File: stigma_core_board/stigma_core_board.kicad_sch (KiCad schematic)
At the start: 83 parts, among them J1 TC2050, J5 USB_C_Receptacle_USB2.0, SW1 KMR721NGLFS, SW2 KMR721NGLFS, U1 STM32H743VITx, U10 H3LIS331DL, U11 MS5607/MS5611, U12 LIS3MDL, U13 BMP580/BMP388/LPS22, U2 TPD4E1U06, U3 BMP580/BMP388/LPS22, U4 IIM-42652 (or other LGA-14 IM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, U5 AZ1117I-3.3, U6 ICM-42688 (or other LGA-14 IM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, U8 W25Q128JVP, U9 LSM6DSR, Y1 25MHz, Y2 32.768kHz

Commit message: Restore stigma_core_board from 4524638
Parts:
- added C39, C40: 100n, Capacitor_SMD:C_0402_1005Metric, symbol Device:C_Small
- added R14: 4k7, Resistor_SMD:R_0402_1005Metric, symbol Device:R_Small
- added R15: 10k, Resistor_SMD:R_0402_1005Metric, symbol Device:R_Small
- added R16, R17, R18, R19, R20: 22, Resistor_SMD:R_0402_1005Metric, symbol Device:R_Small
- added U7: TPD4E1U06, Package_TO_SOT_SMD:SOT-563, symbol stigma:TPD4E001DRL
- C1: LCSC (none) -> C19666
- C10, C9: LCSC (none) -> C12530
- C11, C12: value 3.9p -> 10p; LCSC (none) -> C32949
- C13, C14: value 1.5p -> 10p; LCSC (none) -> C32949
- C15, C20, C21, C22, C24, C25, C27, C28, C29, C30, C31, C34, C35, C36: LCSC (none) -> C1525; LCSC# C1591 -> (none)
- C16, C17, C3, C4, C5, C6, C7: LCSC (none) -> C1525
- C18, C23: LCSC (none) -> C19702; LCSC# C14860 -> (none)
- C19: LCSC (none) -> C86295; LCSC# C12891 -> (none)
- C2, C8: LCSC (none) -> C28323
- C26, C33, C37: LCSC (none) -> C28323; LCSC# C318694 -> (none)
- C32, C38: LCSC (none) -> C15195; LCSC# C1591 -> (none)
- D1: value LED_Small -> red; LCSC (none) -> C2286
- D2: value LED_Small -> yellow; LCSC (none) -> C2296
- D3: value LED_Small -> green; LCSC (none) -> C2297
- D4: footprint Diode_SMD:D_SOD-123F -> Diode_SMD:D_SOD-123; LCSC (none) -> C8598; LCSC# C167645 -> (none)
- FB1: LCSC (none) -> C1002
- J3: footprint stigma:DF40GB-70DP-0.4V -> stigma:DF40GB-70DP-0.4V-plug; symbol Connector_Generic:Conn_02x35_Top_Bottom -> Connector_Generic_Shielded:Conn_02x35_Top_Bottom_Shielded; now left out of the parts list
- J5: LCSC (none) -> C709357; LCSC# C709357 -> (none)
- R1, R2, R3, R4: LCSC (none) -> C17168
- R10, R11: LCSC (none) -> C25905; LCSC# C105580 -> (none)
- R12, R13: value 22 -> 22R; LCSC (none) -> C25092; LCSC# C107701 -> (none)
- R5: LCSC (none) -> C25741; LCSC# C98220 -> (none)
- R6: LCSC (none) -> C11702; LCSC# C98220 -> (none)
- R7, R8, R9: value 680 -> 1k; LCSC (none) -> C11702
- SW1, SW2: LCSC (none) -> C2911418; LCSC# C2911418 -> (none)
- U1: LCSC (none) -> C730183
- U10: LCSC (none) -> C2655074
- U11: LCSC (none) -> C97627
- U12: LCSC (none) -> C478483; LCSC# C478483 -> (none)
- U13: value BMP580/BMP388/LPS22 -> BMP580; LCSC (none) -> C22391138
- U2: footprint Package_TO_SOT_SMD:SOT-23-6 -> Package_TO_SOT_SMD:SOT-563; symbol Power_Protection:SRV05-4 -> stigma:TPD4E001DRL; LCSC (none) -> C527516
- U3: value BMP580/BMP388/LPS22 -> LPS22; LCSC (none) -> C2827824
- U4: value IIM-42652 (or other LGA-14 IMU) -> ICM-42670-P; LCSC (none) -> C3288646; LCSC# C784817 -> (none); Manufacturer STMicroelectronics -> (none); Part# LSM6DSRTR -> (none)
- U5: LCSC (none) -> C92102; LCSC# C92102 -> (none)
- U6: value ICM-42688 (or other LGA-14 IMU) -> ICM-42688-P; LCSC (none) -> C1850418; LCSC# C784817 -> (none)
- U8: LCSC (none) -> C190862
- U9: LCSC (none) -> C784817; LCSC# C784817 -> (none)
- Y1: LCSC (none) -> C9006
- Y2: LCSC (none) -> C70509
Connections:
- net +3V3 is gone; now on net +3.3V: C19.2, C21.2, C22.2, C23.2, C24.2, C25.2, C26.2, C27.2, C29.2, C30.2, C31.2, C32.2, C33.2, C34.2, C35.2, C36.2, C37.2, C38.2, R6.2, U10.1 (VDD_{IO}), U10.14 (VDD), U10.15 (reserved), U11.1 (VDD), U12.5 (Vdd), U12.6 (Vdd_IO), U13.1 (VDDIO), U13.10 (VDD), U3.1 (VDDIO), U3.10 (VDD), U4.5 (VDDIO), U4.8 (VDD), U5.2 (VO), U6.5 (VDDIO), U6.8 (VDD), U9.5 (VDDIO), U9.8 (VDD)
- net ETH_CRS_DV is gone; now on net PA7_ETH_CRS_DV: U1.31 (PA7)
- net ETH_MDC is gone; now on net PC1_ETH_MDC: U1.16 (PC1)
- net ETH_MDIO is gone; now on net PA2_ETH_MDIO: U1.24 (PA2)
- net ETH_RXD0 is gone; now on net ETH_RXD-: U1.32 (PC4)
- net ETH_RXD1 is gone; now on net ETH_RXD+: U1.33 (PC5)
- net ETH_TXD0 is gone; now on net ETH_TXD-: U1.51 (PB12)
- net ETH_TXD1 is gone; now on net ETH_TXD+: U1.52 (PB13)
- net ETH_TX_EN is gone; now on net PB11_ETH_TX_EN: U1.47 (PB11)
- net PA0_U4TX_T2/1_T5/1_ADC is gone; now on net PA0: U1.22 (PA0)
- net PA10_T1/3_U1RX is gone; now on net LED_YELLOW: U1.69 (PA10)
- net PA15_T2/1_U7TX is gone; now on net LED_GREEN: U1.77 (PA15)
- net PA3_U2RX_T2/4_T5/4_T15/2_ADC is gone; now on net PA3: U1.25 (PA3)
- net PA4_ADC_DAC is gone; now on net PA4: U1.28 (PA4)
- net PA8_T1/1_I3SCL_U7RX is gone; now on net LED_RED: U1.67 (PA8)
- net PB0_T1/2N_T3/3_T8/2N_ADC is gone; now on net PB0: U1.34 (PB0)
- net PB10_T2/3_I2SCL_(SPI2_SCK)_U3TX is gone; now on net PB10: U1.46 (PB10)
- net PB1_T1/3N_T3/4_T8/3N_ADC is gone; now on net PB1: U1.35 (PB1)
- net PB4_T3/1_(SPI1_MISO, SPI3_MISO, SPI6_MISO)_U7TX is gone; now on net SPI1_MISO: U1.90 (PB4)
- net PB7_T17/1N_T4/2_I1SDA_I4SDA_U1RX is gone; now on net PB7: U1.93 (PB7)
- net PB8_T16/1_T4/3_I1SCL_I4SCL_U4RX_(CAN1_RX) is gone; now on net PB8: U1.95 (PB8)
- net PB9_T17/1_T4/4_I1SDA_I4SDA_U4TX_(CAN1_TX) is gone; now on net PB9: U1.96 (PB9)
- net SPI1_CS_ACC is gone; now on net SPI1_CS_HIGHG: U10.8 (~{CS})
- net SPI1_CS_BARO2 is gone; now on net SPI2_CS_BARO2: U3.6 (~{CS})
- net SPI1_CS_BARO3 is gone; now on net SPI2_CS_BARO3: U13.6 (~{CS})
- net SPI1_CS_IMU2 is gone; now on net SPI2_CS_IMU2: U6.12 (CS)
- net SPI1_CS_IMU3 is gone; now on net SPI2_CS_IMU3: U4.12 (CS)
- net SPI1_SCL is gone; now on net SPI1_SCK: U10.4 (SCK), U11.8 (SCLK), U12.1 (SCL/SPC), U9.13 (SCL)
- net SPI4_MISO is gone; now on net PE5: U1.4 (PE5)
- net SPI4_MOSI is gone; now on net PE6: U1.5 (PE6)
- net SPI4_SCK is gone; now on net PE2: U1.1 (PE2)
- net +3.3V: now also U7.5 (IO4)
- net +5V: now also J3.1 (Pin_1), J3.2 (Pin_2), J3.34 (Pin_34), J3.35 (Pin_35), J3.36 (Pin_36), J3.37 (Pin_37), J3.69 (Pin_69), J3.70 (Pin_70), C39.2, U7.6 (V_{cc})
- net BOOT: now also U2.1 (IO1), R20.1
- net D0+: now also U2.4 (IO3); no longer U2.6 (IO4)
- net D0-: now also U2.5 (IO4); no longer U2.4 (IO3)
- net GND: now also J3.18 (Pin_18), J3.26 (Pin_26), J3.3 (Pin_3), J3.30 (Pin_30), J3.33 (Pin_33), J3.38 (Pin_38), J3.45 (Pin_45), J3.53 (Pin_53), J3.58 (Pin_58), J3.68 (Pin_68), J3.SH (Shield), U2.3 (GND), C39.1, C40.1, R15.1, U7.3 (GND); no longer J3.25 (Pin_25), J3.28 (Pin_28), J3.44 (Pin_44), J3.60 (Pin_60), U2.2 (VN)
- net NRST: now also U2.2 (IO2), R17.1; no longer U1.14 (NRST)
- net SPI1_CS_BARO1: now also U1.83 (PD2)
- net SPI1_CS_IMU1: now also U1.85 (PD4)
- net SPI1_CS_MAG: now also U1.86 (PD5)
- net SPI1_MISO: no longer U1.30 (PA6)
- net SPI2_MISO: now also U1.53 (PB14); no longer U1.17 (PC2_C)
- net SPI2_MOSI: now also U1.54 (PB15); no longer U1.18 (PC3_C)
- net SPI3_CS_FLASH: now also U1.87 (PD6)
- net SPI3_MISO: now also J3.24 (Pin_24)
- net SPI3_MOSI: now also J3.25 (Pin_25)
- net SPI3_SCK: now also J3.23 (Pin_23)
- net SWCLK: now also R16.2; no longer J1.6 (Pin_6)
- net SWDIO: now also R18.1; no longer J1.2 (Pin_2)
- net SWO: now also R19.1; no longer J1.5 (Pin_5)
- net USB_FS_VBUS: now also R14.1, R15.2
- net VCAP1: now reaches C9.1, U1.48 (VCAP)
- net PC0: now reaches U1.15 (PC0)
- net PC0: now also J3.67 (Pin_67)
- net SPI2_CS_BARO3: now reaches U1.2 (PE3)
- net SPI2_CS_BARO2: now reaches U1.3 (PE4)
- net PE7: now reaches U1.37 (PE7)
- net PE7: now also J3.10 (Pin_10)
- net PE8: now reaches U1.38 (PE8)
- net PE8: now also J3.11 (Pin_11)
- net PE9: now reaches U1.39 (PE9)
- net PE9: now also J3.12 (Pin_12)
- net PE10: now reaches U1.40 (PE10)
- net PE10: now also J3.13 (Pin_13)
- net PE11: now reaches U1.41 (PE11)
- net PE11: now also J3.14 (Pin_14)
- net PE12: now reaches U1.42 (PE12)
- net PE12: now also J3.15 (Pin_15)
- net PE13: now reaches U1.43 (PE13)
- net PE13: now also J3.16 (Pin_16)
- net PE14: now reaches U1.44 (PE14)
- net PE14: now also J3.17 (Pin_17)
- net SPI2_CS_IMU2: now reaches U1.55 (PD8)
- net SPI1_CS_HIGHG: now reaches U1.56 (PD9)
- net PD12: now reaches U1.59 (PD12)
- net PD12: now also J3.41 (Pin_41)
- net PD13: now reaches U1.60 (PD13)
- net PD13: now also J3.42 (Pin_42)
- net PD14: now reaches U1.61 (PD14)
- net PD14: now also J3.43 (Pin_43)
- net PD15: now reaches U1.62 (PD15)
- net PD15: now also J3.44 (Pin_44)
- net PC6: now reaches U1.63 (PC6)
- net PC6: now also J3.19 (Pin_19)
- net PC7: now reaches U1.64 (PC7)
- net PC7: now also J3.20 (Pin_20)
- net PC8: now reaches U1.65 (PC8)
- net PC8: now also J3.21 (Pin_21)
- net PC9: now reaches U1.66 (PC9)
- net PC9: now also J3.22 (Pin_22)
- net SPI2_CS_IMU3: now reaches U1.7 (PC13)
- net VCAP2: now reaches C10.1, U1.73 (VCAP)
- net PD0: now reaches U1.81 (PD0)
- net PD0: now also J3.39 (Pin_39)
- net PD1: now reaches U1.82 (PD1)
- net PD1: now also J3.40 (Pin_40)
- net PB5: now reaches U1.91 (PB5)
- net PB5: now also J3.48 (Pin_48)
- net PB6: now reaches U1.92 (PB6)
- net PB6: now also J3.49 (Pin_49)
- net PE0: now reaches U1.97 (PE0)
- net PE0: now also J3.4 (Pin_4)
- net PE1: now reaches U1.98 (PE1)
- net PE1: now also J3.5 (Pin_5)
- net VBUS: now reaches D4.2 (A), J5.A4 (VBUS), J5.A9 (VBUS), J5.B4 (VBUS), J5.B9 (VBUS)
- net VBUS: now also U2.6 (V_{cc}), C40.2, R14.2; no longer U2.5 (VP)
- net PC1_ETH_MDC: now reaches J3.27 (Pin_27)
- net PC3_C: now reaches J3.29 (Pin_29)
- net PC3_C: now also U1.18 (PC3_C)
- net ETH_RXD-: now reaches J3.31 (Pin_31)
- net ETH_RXD+: now reaches J3.32 (Pin_32)
- net PB0: now reaches J3.46 (Pin_46)
- net PB1: now reaches J3.47 (Pin_47)
- net PB7: now reaches J3.50 (Pin_50)
- net PB8: now reaches J3.51 (Pin_51)
- net PB9: now reaches J3.52 (Pin_52)
- net PB10: now reaches J3.54 (Pin_54)
- net PB11_ETH_TX_EN: now reaches J3.55 (Pin_55)
- net ETH_TXD-: now reaches J3.56 (Pin_56)
- net ETH_TXD+: now reaches J3.57 (Pin_57)
- net PA0: now reaches J3.59 (Pin_59)
- net PE2: now reaches J3.6 (Pin_6)
- net PA2_ETH_MDIO: now reaches J3.61 (Pin_61)
- net PA3: now reaches J3.62 (Pin_62)
- net PA4: now reaches J3.64 (Pin_64)
- net PA6: now reaches J3.65 (Pin_65)
- net PA6: now also U1.30 (PA6)
- net PA7_ETH_CRS_DV: now reaches J3.66 (Pin_66)
- net PE5: now reaches J3.7 (Pin_7)
- net PE6: now reaches J3.8 (Pin_8)
- net BOOT0: no longer names the net of U1.94 (BOOT0)
- net BOOT0: now also R20.2
- net ETH_REF_CLK renamed PA1_ETH_REF_CLK
- net PA1_ETH_REF_CLK: now also J3.60 (Pin_60)
- net PB2_(SPI3_MOSI): no longer names the net of U1.36 (PB2)
- new net: R17.2, U1.14 (NRST)
- new net: J1.6 (Pin_6), R16.1, U7.4 (IO3)
- new net J1-SWDIO: J1.2 (Pin_2), R18.2, U7.2 (IO2)
- new net J1-SWO: J1.5 (Pin_5), R19.2, U7.1 (IO1)
- new net PC2_C: J3.28 (Pin_28), U1.17 (PC2_C)
- no-connect marks 14 -> 18
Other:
- note added: "128 Mbit"
- note added: "flash"
- note removed: "ALSO: T2/2, SPI1_SCK, SPI3_SCK, SPI6_SCK, U7RX"
- note removed: "TODO: ESD protection"
- note removed: "TODO: VBUS detection"
- note removed: "TODO: additional input capacitance?"
- note removed: "TODO: button footprint?"
- note removed: "TODO: clamping diodes for buttons?"
- note removed: "TODO: double check pinout"
- note removed: "TODO: place voltage dividers for battery voltage/current sensing here?"
- note removed: "TODO: replace with BMP585, ICP 20100? Another LGA-10 footprint?"
- moved on the sheet: C15, C18, C19, C20, J1, R5, R6, SW1, SW2, U2, U5, U8

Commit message: uploaded files to share current not working parts
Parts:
- removed C39, C40: 100n, Capacitor_SMD:C_0402_1005Metric, symbol Device:C_Small
- removed R14: 4k7, Resistor_SMD:R_0402_1005Metric, symbol Device:R_Small
- removed R15: 10k, Resistor_SMD:R_0402_1005Metric, symbol Device:R_Small
- removed R16, R17, R18, R19, R20: 22, Resistor_SMD:R_0402_1005Metric, symbol Device:R_Small
- removed U7: TPD4E1U06, Package_TO_SOT_SMD:SOT-563, symbol stigma:TPD4E001DRL
- C1: LCSC C19666 -> (none)
- C10, C9: LCSC C12530 -> (none)
- C11, C12: value 10p -> 3.9p; LCSC C32949 -> (none)
- C13, C14: value 10p -> 1.5p; LCSC C32949 -> (none)
- C15, C20, C21, C22, C24, C25, C27, C28, C29, C30, C31, C34, C35, C36: LCSC C1525 -> (none); LCSC# (none) -> C1591
- C16, C17, C3, C4, C5, C6, C7: LCSC C1525 -> (none)
- C18, C23: LCSC C19702 -> (none); LCSC# (none) -> C14860
- C19: LCSC C86295 -> (none); LCSC# (none) -> C12891
- C2, C8: LCSC C28323 -> (none)
- C26, C33, C37: LCSC C28323 -> (none); LCSC# (none) -> C318694
- C32, C38: LCSC C15195 -> (none); LCSC# (none) -> C1591
- D1: value red -> LED_Small; LCSC C2286 -> (none)
- D2: value yellow -> LED_Small; LCSC C2296 -> (none)
- D3: value green -> LED_Small; LCSC C2297 -> (none)
- D4: footprint Diode_SMD:D_SOD-123 -> Diode_SMD:D_SOD-123F; LCSC C8598 -> (none); LCSC# (none) -> C167645
- FB1: LCSC C1002 -> (none)
- J3: footprint stigma:DF40GB-70DP-0.4V-plug -> stigma:DF40GB-70DP-0.4V; symbol Connector_Generic_Shielded:Conn_02x35_Top_Bottom_Shielded -> Connector_Generic:Conn_02x35_Top_Bottom; now in the parts list
- J5: LCSC C709357 -> (none); LCSC# (none) -> C709357
- R1, R2, R3, R4: LCSC C17168 -> (none)
- R10, R11: LCSC C25905 -> (none); LCSC# (none) -> C105580
- R12, R13: value 22R -> 22; LCSC C25092 -> (none); LCSC# (none) -> C107701
- R5: LCSC C25741 -> (none); LCSC# (none) -> C98220
- R6: LCSC C11702 -> (none); LCSC# (none) -> C98220
- R7, R8, R9: value 1k -> 680; LCSC C11702 -> (none)
- SW1, SW2: LCSC C2911418 -> (none); LCSC# (none) -> C2911418
- U1: LCSC C730183 -> (none)
- U10: LCSC C2655074 -> (none)
- U11: LCSC C97627 -> (none)
- U12: LCSC C478483 -> (none); LCSC# (none) -> C478483
- U13: value BMP580 -> BMP580/BMP388/LPS22; LCSC C22391138 -> (none)
- U2: footprint Package_TO_SOT_SMD:SOT-563 -> Package_TO_SOT_SMD:SOT-23-6; symbol stigma:TPD4E001DRL -> Power_Protection:SRV05-4; LCSC C527516 -> (none)
- U3: value LPS22 -> BMP580/BMP388/LPS22; LCSC C2827824 -> (none)
- U4: value ICM-42670-P -> IIM-42652 (or other LGA-14 IMU); LCSC C3288646 -> (none); LCSC# (none) -> C784817; Manufacturer (none) -> STMicroelectronics; Part# (none) -> LSM6DSRTR
- U5: LCSC C92102 -> (none); LCSC# (none) -> C92102
- U6: value ICM-42688-P -> ICM-42688 (or other LGA-14 IMU); LCSC C1850418 -> (none); LCSC# (none) -> C784817
- U8: LCSC C190862 -> (none)
- U9: LCSC C784817 -> (none); LCSC# (none) -> C784817
- Y1: LCSC C9006 -> (none)
- Y2: LCSC C70509 -> (none)
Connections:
- net J1-SWDIO is gone; now on net SWDIO: J1.2 (Pin_2)
- net J1-SWO is gone; now on net SWO: J1.5 (Pin_5)
- net +3.3V: no longer C19.2, C21.2, C22.2, C23.2, C24.2, C25.2, C26.2, C27.2, C29.2, C30.2, C31.2, C32.2, C33.2, C34.2, C35.2, C36.2, C37.2, C38.2, R6.2, U10.1 (VDD_{IO}), U10.14 (VDD), U10.15 (reserved), U11.1 (VDD), U12.5 (Vdd), U12.6 (Vdd_IO), U13.1 (VDDIO), U13.10 (VDD), U3.1 (VDDIO), U3.10 (VDD), U4.5 (VDDIO), U4.8 (VDD), U5.2 (VO), U6.5 (VDDIO), U6.8 (VDD), U9.5 (VDDIO), U9.8 (VDD)
- net +5V: no longer J3.1 (Pin_1), J3.2 (Pin_2), J3.34 (Pin_34), J3.35 (Pin_35), J3.36 (Pin_36), J3.37 (Pin_37), J3.69 (Pin_69), J3.70 (Pin_70)
- net BOOT: no longer U2.1 (IO1)
- net D0+: now also U2.6 (IO4); no longer U2.4 (IO3)
- net D0-: now also U2.4 (IO3); no longer U2.5 (IO4)
- net GND: now also J3.25 (Pin_25), J3.28 (Pin_28), J3.44 (Pin_44), J3.60 (Pin_60), U2.2 (VN); no longer J3.18 (Pin_18), J3.26 (Pin_26), J3.3 (Pin_3), J3.30 (Pin_30), J3.33 (Pin_33), J3.38 (Pin_38), J3.45 (Pin_45), J3.53 (Pin_53), J3.58 (Pin_58), J3.68 (Pin_68), J3.SH (Shield), U2.3 (GND)
- net LED_GREEN: no longer U1.77 (PA15)
- net LED_RED: no longer U1.67 (PA8)
- net LED_YELLOW: no longer U1.69 (PA10)
- net NRST: now also U1.14 (NRST); no longer U2.2 (IO2)
- net SPI1_CS_BARO1: no longer U1.83 (PD2)
- net SPI1_CS_IMU1: no longer U1.85 (PD4)
- net SPI1_CS_MAG: no longer U1.86 (PD5)
- net SPI1_MISO: now also U1.30 (PA6); no longer U1.90 (PB4)
- net SPI1_SCK: no longer U10.4 (SCK), U11.8 (SCLK), U12.1 (SCL/SPC), U9.13 (SCL)
- net SPI2_MISO: now also U1.17 (PC2_C); no longer U1.53 (PB14)
- net SPI2_MOSI: now also U1.18 (PC3_C); no longer U1.54 (PB15)
- net SPI3_CS_FLASH: no longer U1.87 (PD6)
- net SPI3_MISO: no longer J3.24 (Pin_24)
- net SPI3_MOSI: no longer J3.25 (Pin_25)
- net SPI3_SCK: no longer J3.23 (Pin_23)
- net SWCLK: now also J1.6 (Pin_6)
- net PB2_(SPI3_MOSI): now reaches U1.36 (PB2)
- net BOOT0: now reaches U1.94 (BOOT0)
- net ETH_RXD+: no longer names the net of J3.32 (Pin_32)
- net ETH_RXD+: no longer U1.33 (PC5)
- net ETH_RXD-: no longer names the net of J3.31 (Pin_31)
- net ETH_RXD-: no longer U1.32 (PC4)
- net ETH_TXD+: no longer names the net of J3.57 (Pin_57)
- net ETH_TXD+: no longer U1.52 (PB13)
- net ETH_TXD-: no longer names the net of J3.56 (Pin_56)
- net ETH_TXD-: no longer U1.51 (PB12)
- net PA0: no longer names the net of J3.59 (Pin_59)
- net PA0: no longer U1.22 (PA0)
- net PA1_ETH_REF_CLK renamed ETH_REF_CLK
- net ETH_REF_CLK: no longer J3.60 (Pin_60)
- net PA2_ETH_MDIO: no longer names the net of J3.61 (Pin_61)
- net PA2_ETH_MDIO: no longer U1.24 (PA2)
- net PA3: no longer names the net of J3.62 (Pin_62)
- net PA3: no longer U1.25 (PA3)
- net PA4: no longer names the net of J3.64 (Pin_64)
- net PA4: no longer U1.28 (PA4)
- net PA6: no longer names the net of J3.65 (Pin_65)
- net PA6: no longer U1.30 (PA6)
- net PA7_ETH_CRS_DV: no longer names the net of J3.66 (Pin_66)
- net PA7_ETH_CRS_DV: no longer U1.31 (PA7)
- net PB0: no longer names the net of J3.46 (Pin_46)
- net PB0: no longer U1.34 (PB0)
- net PB1: no longer names the net of J3.47 (Pin_47)
- net PB1: no longer U1.35 (PB1)
- net PB10: no longer names the net of J3.54 (Pin_54)
- net PB10: no longer U1.46 (PB10)
- net PB11_ETH_TX_EN: no longer names the net of J3.55 (Pin_55)
- net PB11_ETH_TX_EN: no longer U1.47 (PB11)
- net PB5: no longer names the net of U1.91 (PB5)
- net PB5: no longer J3.48 (Pin_48)
- net PB6: no longer names the net of U1.92 (PB6)
- net PB6: no longer J3.49 (Pin_49)
- net PB7: no longer names the net of J3.50 (Pin_50)
- net PB7: no longer U1.93 (PB7)
- net PB8: no longer names the net of J3.51 (Pin_51)
- net PB8: no longer U1.95 (PB8)
- net PB9: no longer names the net of J3.52 (Pin_52)
- net PB9: no longer U1.96 (PB9)
- net PC0: no longer names the net of U1.15 (PC0)
- net PC0: no longer J3.67 (Pin_67)
- net PC1_ETH_MDC: no longer names the net of J3.27 (Pin_27)
- net PC1_ETH_MDC: no longer U1.16 (PC1)
- removed net PC2_C: J3.28 (Pin_28), U1.17 (PC2_C)
- net PC3_C: no longer names the net of J3.29 (Pin_29)
- net PC3_C: no longer U1.18 (PC3_C)
- net PC6: no longer names the net of U1.63 (PC6)
- net PC6: no longer J3.19 (Pin_19)
- net PC7: no longer names the net of U1.64 (PC7)
- net PC7: no longer J3.20 (Pin_20)
- net PC8: no longer names the net of U1.65 (PC8)
- net PC8: no longer J3.21 (Pin_21)
- net PC9: no longer names the net of U1.66 (PC9)
- net PC9: no longer J3.22 (Pin_22)
- net PD0: no longer names the net of U1.81 (PD0)
- net PD0: no longer J3.39 (Pin_39)
- net PD1: no longer names the net of U1.82 (PD1)
- net PD1: no longer J3.40 (Pin_40)
- net PD12: no longer names the net of U1.59 (PD12)
- net PD12: no longer J3.41 (Pin_41)
- net PD13: no longer names the net of U1.60 (PD13)
- net PD13: no longer J3.42 (Pin_42)
- net PD14: no longer names the net of U1.61 (PD14)
- net PD14: no longer J3.43 (Pin_43)
- net PD15: no longer names the net of U1.62 (PD15)
- net PD15: no longer J3.44 (Pin_44)
- net PE0: no longer names the net of U1.97 (PE0)
- net PE0: no longer J3.4 (Pin_4)
- net PE1: no longer names the net of U1.98 (PE1)
- net PE1: no longer J3.5 (Pin_5)
- net PE10: no longer names the net of U1.40 (PE10)
- net PE10: no longer J3.13 (Pin_13)
- net PE11: no longer names the net of U1.41 (PE11)
- net PE11: no longer J3.14 (Pin_14)
- net PE12: no longer names the net of U1.42 (PE12)
- net PE12: no longer J3.15 (Pin_15)
- net PE13: no longer names the net of U1.43 (PE13)
- net PE13: no longer J3.16 (Pin_16)
- net PE14: no longer names the net of U1.44 (PE14)
- net PE14: no longer J3.17 (Pin_17)
- net PE2: no longer names the net of J3.6 (Pin_6)
- net PE2: no longer U1.1 (PE2)
- net PE5: no longer names the net of J3.7 (Pin_7)
- net PE5: no longer U1.4 (PE5)
- net PE6: no longer names the net of J3.8 (Pin_8)
- net PE6: no longer U1.5 (PE6)
- net PE7: no longer names the net of U1.37 (PE7)
- net PE7: no longer J3.10 (Pin_10)
- net PE8: no longer names the net of U1.38 (PE8)
- net PE8: no longer J3.11 (Pin_11)
- net PE9: no longer names the net of U1.39 (PE9)
- net PE9: no longer J3.12 (Pin_12)
- net SPI1_CS_HIGHG: no longer names the net of U1.56 (PD9)
- net SPI1_CS_HIGHG: no longer U10.8 (~{CS})
- net SPI2_CS_BARO2: no longer names the net of U1.3 (PE4)
- net SPI2_CS_BARO2: no longer U3.6 (~{CS})
- net SPI2_CS_BARO3: no longer names the net of U1.2 (PE3)
- net SPI2_CS_BARO3: no longer U13.6 (~{CS})
- net SPI2_CS_IMU2: no longer names the net of U1.55 (PD8)
- net SPI2_CS_IMU2: no longer U6.12 (CS)
- net SPI2_CS_IMU3: no longer names the net of U1.7 (PC13)
- net SPI2_CS_IMU3: no longer U4.12 (CS)
- net VBUS: no longer names the net of D4.2 (A), J5.A4 (VBUS), J5.A9 (VBUS), J5.B4 (VBUS), J5.B9 (VBUS)
- net VBUS: now also U2.5 (VP); no longer U2.6 (V_{cc})
- net VCAP1: no longer names the net of C9.1, U1.48 (VCAP)
- net VCAP2: no longer names the net of C10.1, U1.73 (VCAP)
- new net +3V3: C19.2, C21.2, C22.2, C23.2, C24.2, C25.2, C26.2, C27.2, C29.2, C30.2, C31.2, C32.2, C33.2, C34.2, C35.2, C36.2, C37.2, C38.2, R6.2, U10.1 (VDD_{IO}), U10.14 (VDD), U10.15 (reserved), U11.1 (VDD), U12.5 (Vdd), U12.6 (Vdd_IO), U13.1 (VDDIO), U13.10 (VDD), U3.1 (VDDIO), U3.10 (VDD), U4.5 (VDDIO), U4.8 (VDD), U5.2 (VO), U6.5 (VDDIO), U6.8 (VDD), U9.5 (VDDIO), U9.8 (VDD)
- new net ETH_CRS_DV: U1.31 (PA7)
- new net ETH_MDC: U1.16 (PC1)
- new net ETH_MDIO: U1.24 (PA2)
- new net ETH_RXD0: U1.32 (PC4)
- new net ETH_RXD1: U1.33 (PC5)
- new net ETH_TXD0: U1.51 (PB12)
- new net ETH_TXD1: U1.52 (PB13)
- new net ETH_TX_EN: U1.47 (PB11)
- new net PA0_U4TX_T2/1_T5/1_ADC: U1.22 (PA0)
- new net PA10_T1/3_U1RX: U1.69 (PA10)
- new net PA15_T2/1_U7TX: U1.77 (PA15)
- new net PA3_U2RX_T2/4_T5/4_T15/2_ADC: U1.25 (PA3)
- new net PA4_ADC_DAC: U1.28 (PA4)
- new net PA8_T1/1_I3SCL_U7RX: U1.67 (PA8)
- new net PB0_T1/2N_T3/3_T8/2N_ADC: U1.34 (PB0)
- new net PB10_T2/3_I2SCL_(SPI2_SCK)_U3TX: U1.46 (PB10)
- new net PB1_T1/3N_T3/4_T8/3N_ADC: U1.35 (PB1)
- new net PB4_T3/1_(SPI1_MISO, SPI3_MISO, SPI6_MISO)_U7TX: U1.90 (PB4)
- new net PB7_T17/1N_T4/2_I1SDA_I4SDA_U1RX: U1.93 (PB7)
- new net PB8_T16/1_T4/3_I1SCL_I4SCL_U4RX_(CAN1_RX): U1.95 (PB8)
- new net PB9_T17/1_T4/4_I1SDA_I4SDA_U4TX_(CAN1_TX): U1.96 (PB9)
- new net SPI1_CS_ACC: U10.8 (~{CS})
- new net SPI1_CS_BARO2: U3.6 (~{CS})
- new net SPI1_CS_BARO3: U13.6 (~{CS})
- new net SPI1_CS_IMU2: U6.12 (CS)
- new net SPI1_CS_IMU3: U4.12 (CS)
- new net SPI1_SCL: U10.4 (SCK), U11.8 (SCLK), U12.1 (SCL/SPC), U9.13 (SCL)
- new net SPI4_MISO: U1.4 (PE5)
- new net SPI4_MOSI: U1.5 (PE6)
- new net SPI4_SCK: U1.1 (PE2)
- no-connect marks 18 -> 14
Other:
- note added: "ALSO: T2/2, SPI1_SCK, SPI3_SCK, SPI6_SCK, U7RX"
- note added: "TODO: ESD protection"
- note added: "TODO: VBUS detection"
- note added: "TODO: additional input capacitance?"
- note added: "TODO: button footprint?"
- note added: "TODO: clamping diodes for buttons?"
- note added: "TODO: double check pinout"
- note added: "TODO: place voltage dividers for battery voltage/current sensing here?"
- note added: "TODO: replace with BMP585, ICP 20100? Another LGA-10 footprint?"
- note removed: "128 Mbit"
- note removed: "flash"
- moved on the sheet: C15, C18, C19, C20, J1, R5, R6, SW1, SW2, U2, U5, U8

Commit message: Clean up previous pinout attempt
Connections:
- net ETH_TX_EN is gone; now on net PB11: U1.47 (PB11)
- net PB4_T3/1_(SPI1_MISO, SPI3_MISO, SPI6_MISO)_U7TX is gone; now on net SPI1_MISO: U1.90 (PB4)
- net SPI1_SCL is gone; now on net SPI1_SCK: U10.4 (SCK), U11.8 (SCLK), U12.1 (SCL/SPC), U9.13 (SCL)
- net GND: no longer J3.25 (Pin_25), J3.28 (Pin_28), J3.44 (Pin_44), J3.60 (Pin_60), J3.63 (Pin_63), J3.9 (Pin_9)
- net SPI1_MISO: no longer U1.30 (PA6)
- net SPI2_MISO: now also U1.53 (PB14); no longer U1.17 (PC2_C)
- net SPI2_MOSI: now also U1.54 (PB15); no longer U1.18 (PC3_C)
- net SPI3_CS_FLASH: now also U1.7 (PC13)
- net PB11: now reaches J3.55 (Pin_55)
- net ETH_CRS_DV: no longer names the net of U1.31 (PA7)
- net ETH_MDC: no longer names the net of U1.16 (PC1)
- net ETH_MDIO: no longer names the net of U1.24 (PA2)
- net ETH_REF_CLK: no longer names the net of U1.23 (PA1)
- net ETH_RXD0: no longer names the net of U1.32 (PC4)
- net ETH_RXD1: no longer names the net of U1.33 (PC5)
- net ETH_TXD0: no longer names the net of U1.51 (PB12)
- net ETH_TXD1: no longer names the net of U1.52 (PB13)
- net PA0_U4TX_T2/1_T5/1_ADC: no longer names the net of U1.22 (PA0)
- net PA10_T1/3_U1RX: no longer names the net of U1.69 (PA10)
- net PA15_T2/1_U7TX: no longer names the net of U1.77 (PA15)
- net PA3_U2RX_T2/4_T5/4_T15/2_ADC: no longer names the net of U1.25 (PA3)
- net PA4_ADC_DAC: no longer names the net of U1.28 (PA4)
- net PA8_T1/1_I3SCL_U7RX: no longer names the net of U1.67 (PA8)
- net PB0_T1/2N_T3/3_T8/2N_ADC: no longer names the net of U1.34 (PB0)
- net PB10_T2/3_I2SCL_(SPI2_SCK)_U3TX: no longer names the net of U1.46 (PB10)
- net PB1_T1/3N_T3/4_T8/3N_ADC: no longer names the net of U1.35 (PB1)
- net PB2_(SPI3_MOSI): no longer names the net of U1.36 (PB2)
- net PB7_T17/1N_T4/2_I1SDA_I4SDA_U1RX: no longer names the net of U1.93 (PB7)
- net PB8_T16/1_T4/3_I1SCL_I4SCL_U4RX_(CAN1_RX): no longer names the net of U1.95 (PB8)
- net PB9_T17/1_T4/4_I1SDA_I4SDA_U4TX_(CAN1_TX): no longer names the net of U1.96 (PB9)
- net SPI1_CS_ACC renamed SPI1_CS_HIGHG
- net SPI1_CS_BARO2 renamed SPI2_CS_BARO2
- net SPI1_CS_BARO3 renamed SPI2_CS_BARO3
- net SPI1_CS_IMU2 renamed SPI2_CS_IMU2
- net SPI1_CS_IMU3 renamed SPI2_CS_IMU3
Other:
- note removed: "ALSO: T2/2, SPI1_SCK, SPI3_SCK, SPI6_SCK, U7RX"
- moved on the sheet: J3

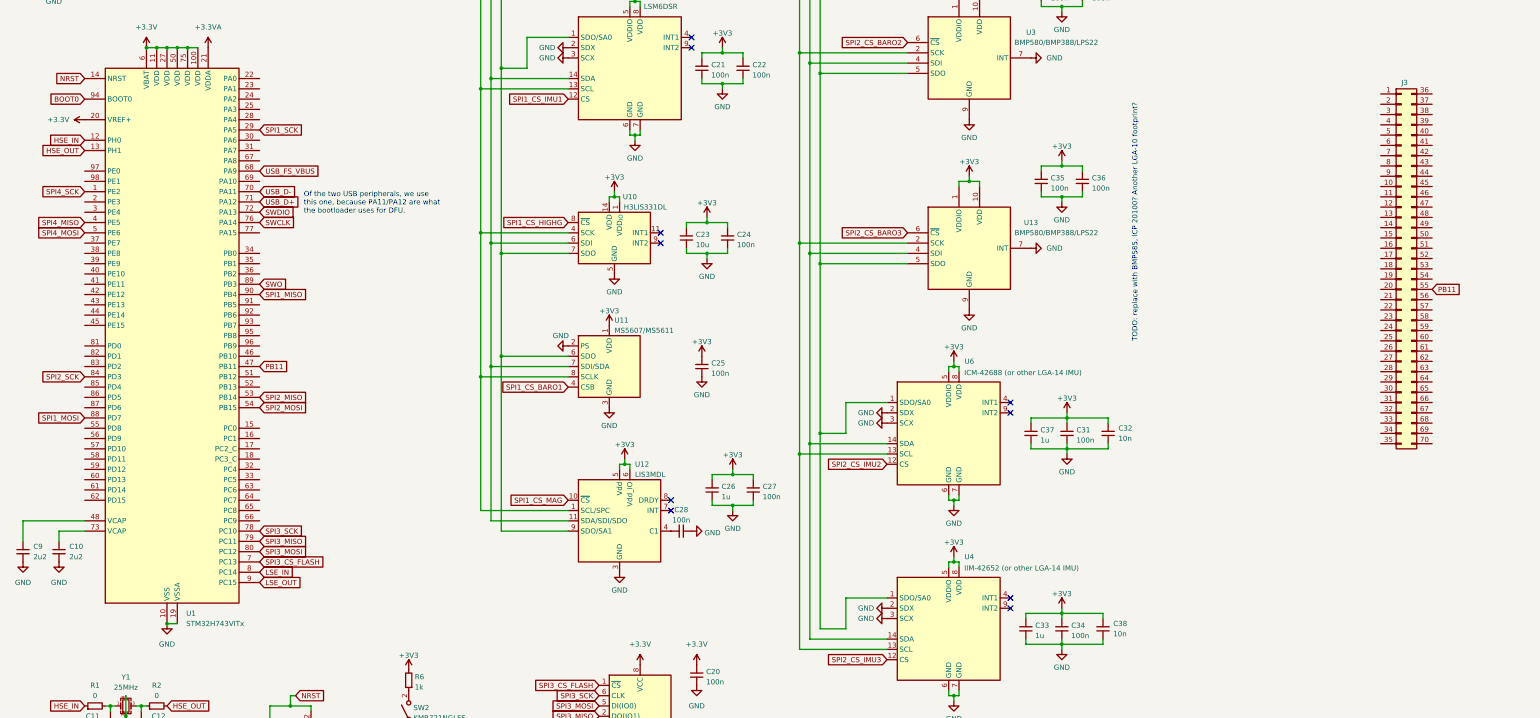
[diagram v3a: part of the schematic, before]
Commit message: added stm32 and connector pinout
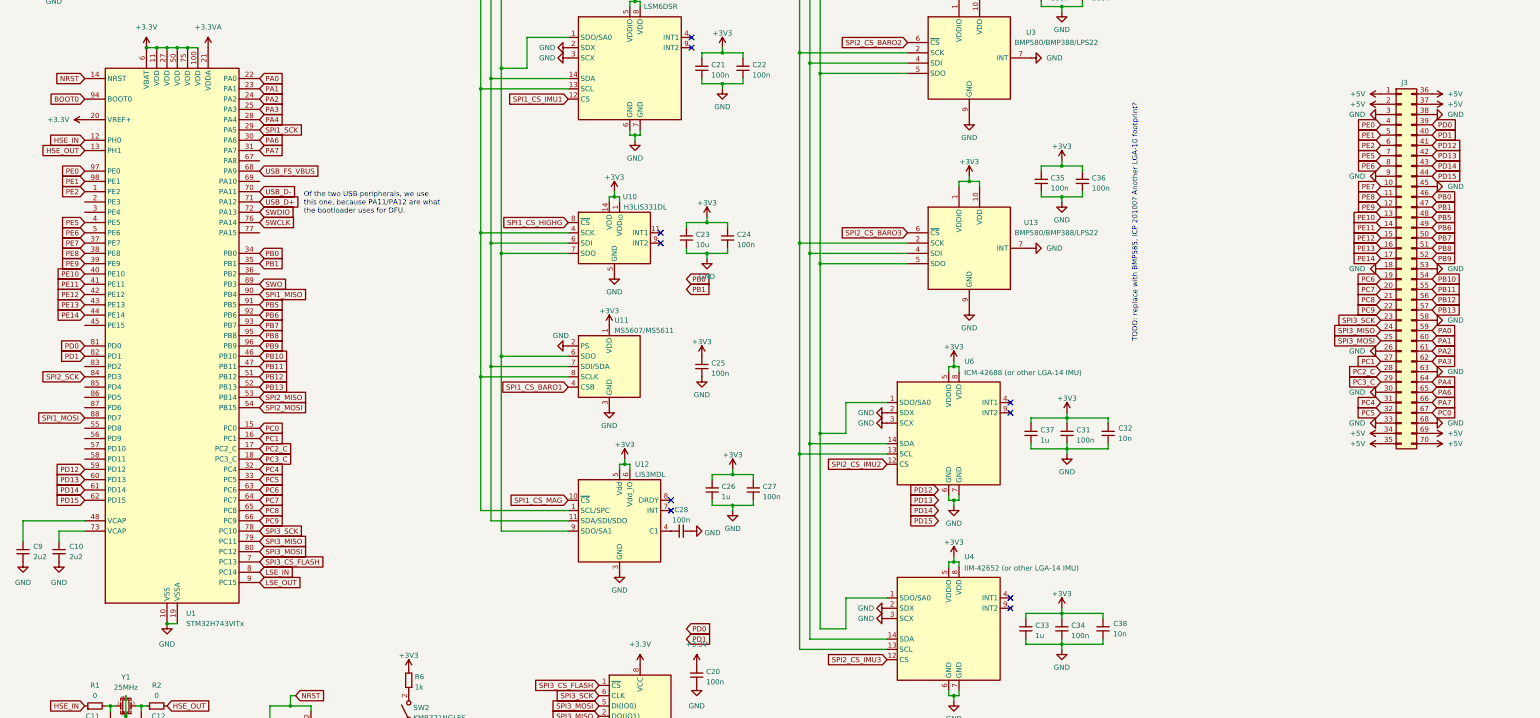
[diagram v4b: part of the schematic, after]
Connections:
- net SPI4_MISO is gone; now on net PE5: U1.4 (PE5)
- net SPI4_MOSI is gone; now on net PE6: U1.5 (PE6)
- net SPI4_SCK is gone; now on net PE2: U1.1 (PE2)
- net +5V: now also J3.1 (Pin_1), J3.2 (Pin_2), J3.34 (Pin_34), J3.35 (Pin_35), J3.36 (Pin_36), J3.37 (Pin_37), J3.69 (Pin_69), J3.70 (Pin_70)
- net GND: now also J3.18 (Pin_18), J3.26 (Pin_26), J3.3 (Pin_3), J3.30 (Pin_30), J3.33 (Pin_33), J3.38 (Pin_38), J3.45 (Pin_45), J3.53 (Pin_53), J3.58 (Pin_58), J3.63 (Pin_63), J3.68 (Pin_68), J3.9 (Pin_9)
- net SPI3_MISO: now also J3.24 (Pin_24)
- net SPI3_MOSI: now also J3.25 (Pin_25)
- net SPI3_SCK: now also J3.23 (Pin_23)
- net PC0: now reaches U1.15 (PC0)
- net PC0: now also J3.67 (Pin_67)
- net PC1: now reaches U1.16 (PC1)
- net PC1: now also J3.27 (Pin_27)
- net PC2_C: now reaches U1.17 (PC2_C)
- net PC2_C: now also J3.28 (Pin_28)
- net PC3_C: now reaches U1.18 (PC3_C)
- net PC3_C: now also J3.29 (Pin_29)
- net PA0: now reaches U1.22 (PA0)
- net PA0: now also J3.59 (Pin_59)
- net PA1: now reaches U1.23 (PA1)
- net PA1: now also J3.60 (Pin_60)
- net PA2: now reaches U1.24 (PA2)
- net PA2: now also J3.61 (Pin_61)
- net PA3: now reaches U1.25 (PA3)
- net PA3: now also J3.62 (Pin_62)
- net PA4: now reaches U1.28 (PA4)
- net PA4: now also J3.64 (Pin_64)
- net PA6: now reaches U1.30 (PA6)
- net PA6: now also J3.65 (Pin_65)
- net PA7: now reaches U1.31 (PA7)
- net PA7: now also J3.66 (Pin_66)
- net PC4: now reaches U1.32 (PC4)
- net PC4: now also J3.31 (Pin_31)
- net PC5: now reaches U1.33 (PC5)
- net PC5: now also J3.32 (Pin_32)
- net PB0: now reaches U1.34 (PB0)
- net PB0: now also J3.46 (Pin_46)
- net PB1: now reaches U1.35 (PB1)
- net PB1: now also J3.47 (Pin_47)
- net PE7: now reaches U1.37 (PE7)
- net PE7: now also J3.10 (Pin_10)
- net PE8: now reaches U1.38 (PE8)
- net PE8: now also J3.11 (Pin_11)
- net PE9: now reaches U1.39 (PE9)
- net PE9: now also J3.12 (Pin_12)
- net PE10: now reaches U1.40 (PE10)
- net PE10: now also J3.13 (Pin_13)
- net PE11: now reaches U1.41 (PE11)
- net PE11: now also J3.14 (Pin_14)
- net PE12: now reaches U1.42 (PE12)
- net PE12: now also J3.15 (Pin_15)
- net PE13: now reaches U1.43 (PE13)
- net PE13: now also J3.16 (Pin_16)
- net PE14: now reaches U1.44 (PE14)
- net PE14: now also J3.17 (Pin_17)
- net PB10: now reaches U1.46 (PB10)
- net PB10: now also J3.54 (Pin_54)
- net PB12: now reaches U1.51 (PB12)
- net PB12: now also J3.56 (Pin_56)
- net PB13: now reaches U1.52 (PB13)
- net PB13: now also J3.57 (Pin_57)
- net PD12: now reaches U1.59 (PD12)
- net PD12: now also J3.41 (Pin_41)
- net PD13: now reaches U1.60 (PD13)
- net PD13: now also J3.42 (Pin_42)
- net PD14: now reaches U1.61 (PD14)
- net PD14: now also J3.43 (Pin_43)
- net PD15: now reaches U1.62 (PD15)
- net PD15: now also J3.44 (Pin_44)
- net PC6: now reaches U1.63 (PC6)
- net PC6: now also J3.19 (Pin_19)
- net PC7: now reaches U1.64 (PC7)
- net PC7: now also J3.20 (Pin_20)
- net PC8: now reaches U1.65 (PC8)
- net PC8: now also J3.21 (Pin_21)
- net PC9: now reaches U1.66 (PC9)
- net PC9: now also J3.22 (Pin_22)
- net PD0: now reaches U1.81 (PD0)
- net PD0: now also J3.39 (Pin_39)
- net PD1: now reaches U1.82 (PD1)
- net PD1: now also J3.40 (Pin_40)
- net PB5: now reaches U1.91 (PB5)
- net PB5: now also J3.48 (Pin_48)
- net PB6: now reaches U1.92 (PB6)
- net PB6: now also J3.49 (Pin_49)
- net PB7: now reaches U1.93 (PB7)
- net PB7: now also J3.50 (Pin_50)
- net PB8: now reaches U1.95 (PB8)
- net PB8: now also J3.51 (Pin_51)
- net PB9: now reaches U1.96 (PB9)
- net PB9: now also J3.52 (Pin_52)
- net PE0: now reaches U1.97 (PE0)
- net PE0: now also J3.4 (Pin_4)
- net PE1: now reaches U1.98 (PE1)
- net PE1: now also J3.5 (Pin_5)
- net PE2: now reaches J3.6 (Pin_6)
- net PE5: now reaches J3.7 (Pin_7)
- net PE6: now reaches J3.8 (Pin_8)
